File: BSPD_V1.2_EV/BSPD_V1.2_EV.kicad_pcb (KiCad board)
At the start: 2 copper layers, 82.1 x 92.5 mm, 64 parts, among them IC1 LM2901BIRTER, IC2 LM2901BIRTER, IC3 74AHC1G08, IC4 SN74HC32PWR, IC5 L7805ACD2T-TR, J1 776280-1, Q1 2N7002,215

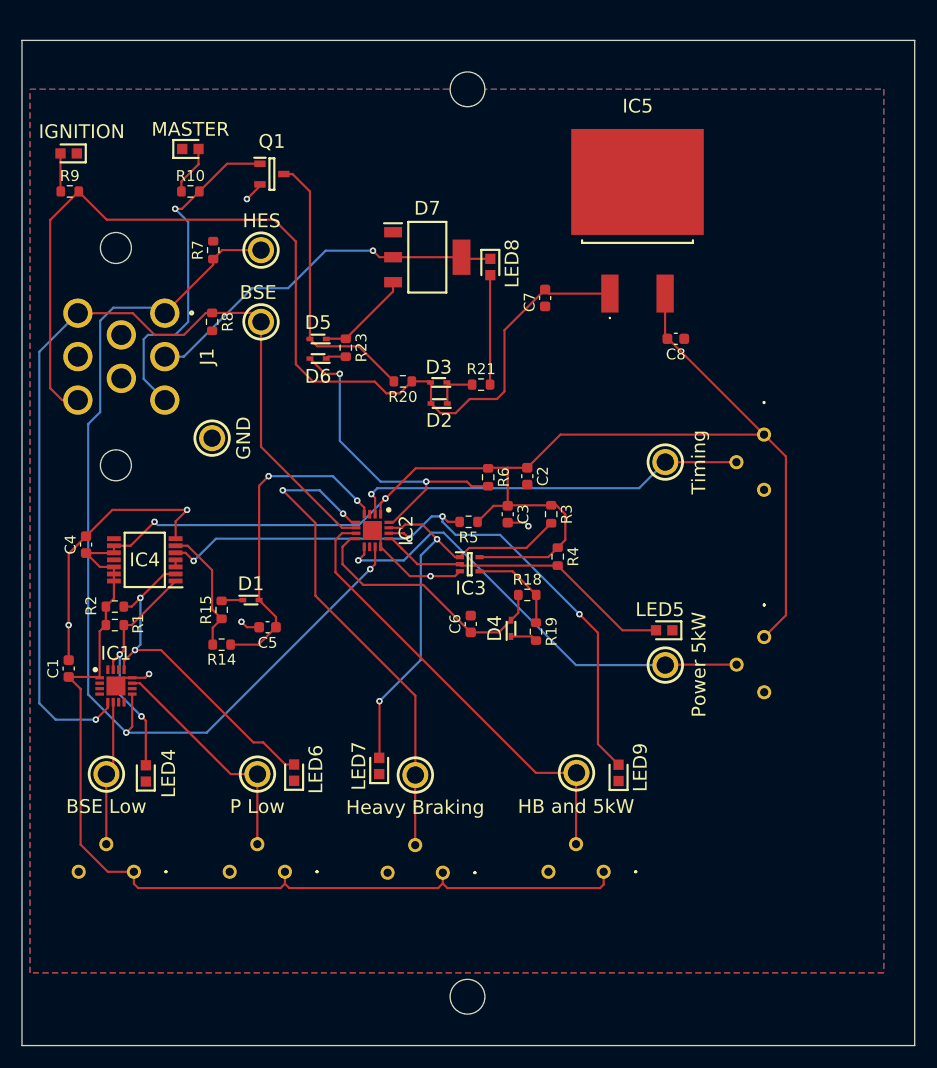
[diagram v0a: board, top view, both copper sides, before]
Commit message: BSPD, Shutdown/Charging Shutdown, & Voltage Indicator final changes
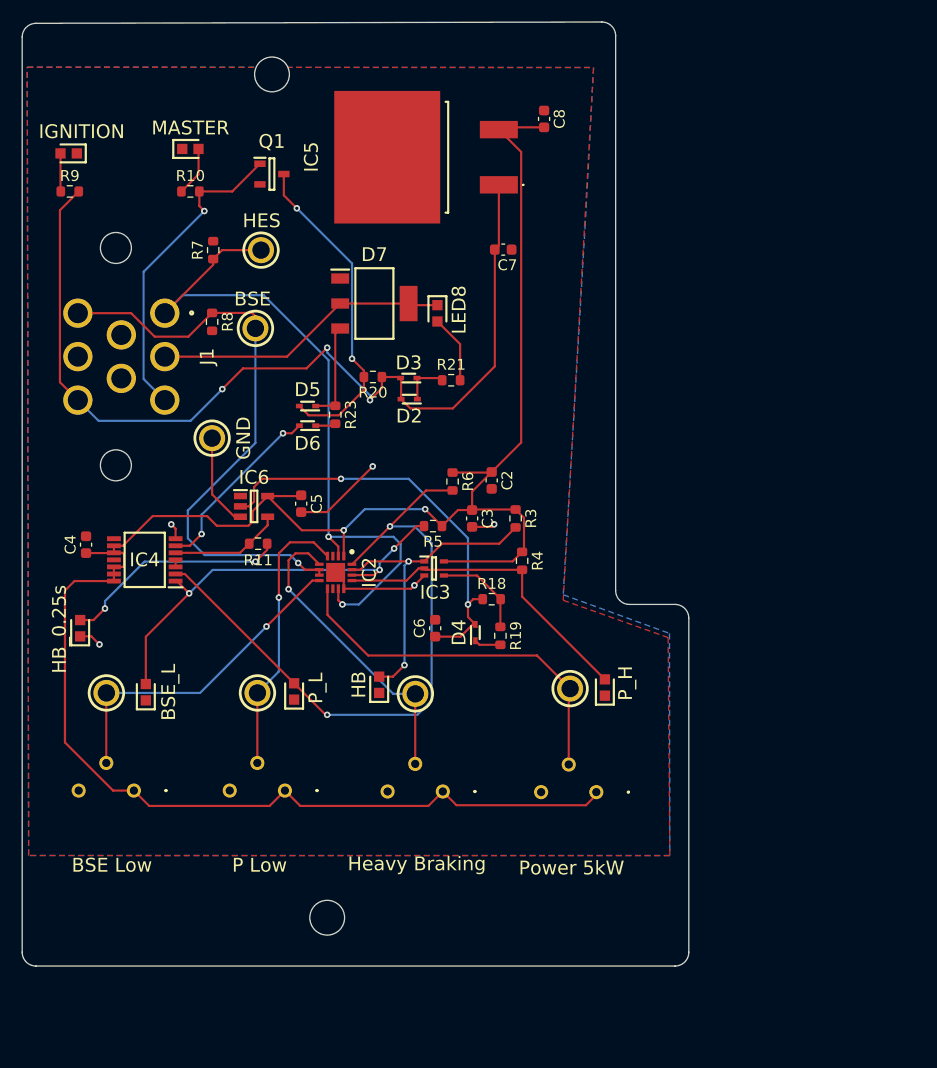
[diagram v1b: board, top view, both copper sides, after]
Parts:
- removed C1: 1uF, Capacitor_SMD:C_0603_1608Metric
- removed D1: BAT54XV2T1G, SDM_MiscFootprint:SODFL1608X70N
- removed IC1: LM2901BIRTER, SDM_MiscFootprint:QFN50P300X300X80-17N-D
- removed R1, R2: 220, Resistor_SMD:R_0603_1608Metric
- removed R14: 10k, Resistor_SMD:R_0603_1608Metric
- removed R15: 100, Resistor_SMD:R_0603_1608Metric
- removed RED_TP1, RED_TP2: 5005, SDM_MiscFootprint:5005
- removed the REF** at (102.7, 155.1)
- removed the REF** at (102.7, 71.6)
- removed VR1, VR2: 10k, SDM_MiscFootprint:3386P1103TLF
- added IC6: SN74LVC1G17DBVRG4, Misc:SOT95P280X145-5N, F.Cu at (83.1, 110.0)
- added R11: 220, Resistor_SMD:R_0603_1608Metric, F.Cu at (83.4, 113.4)
- added REF**: MountingHole_3.2mm_M3, MountingHole:MountingHole_3.2mm_M3, F.Cu at (84.7, 70.2)
- added REF**: MountingHole_3.2mm_M3, MountingHole:MountingHole_3.2mm_M3, F.Cu at (89.8, 147.8)
- C5: value 10uF -> 1uF
- R18: value 50k -> 25k
- moved HB_0.25s 51.3 mm to (67.1, 121.2)
- moved C8 23.6 mm to (109.7, 74.3), turned to -90 degrees
- moved VR3 21.0 mm to (114.6, 136.3), turned to 0 degrees
- moved IC5 20.5 mm to (98.7, 77.9), turned to 90 degrees
- moved C5 11.8 mm to (87.4, 109.7), turned to -90 degrees
- moved RED_TP3 9.02 mm to (112.1, 126.7), turned to 0 degrees
- moved P_H 7.58 mm to (115.3, 126.6), turned to 90 degrees
- moved BSE_L 7.47 mm to (73.1, 127.1)
- moved HB 7.47 mm to (94.6, 126.4)
- moved RED_TP5 7.47 mm to (83.4, 127.1)
- moved RED_TP6 7.47 mm to (69.5, 127.1)
- moved VR4 7.47 mm to (100.4, 136.2)
- moved VR5 7.47 mm to (85.9, 136.1)
- moved VR6 7.47 mm to (72.0, 136.1)
- moved P_L 7.47 mm to (86.7, 127.0)
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- renumbered LED4 to BSE_L, LED7 to HB, LED9 to HB_0.25s, LED5 to P_H, LED6 to P_L
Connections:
- C5 pad 1: /BL+PL+(HB*5kW)_FAULT -> +5V
- HB_0.25s pad 2: /HB*5kW_0.25s_FAULT -> Net-(LED9-A)
- IC2 pad 14: /HB*5kW_0.25s_FAULT -> /BSE_LOW_FAULT
- IC2 pad 16: /BSPD_LOGIC_SIGNAL -> /P_LOW_FAULT
- IC2 pad 2: /TIMING_REF -> /P_MAIN
- IC2 pad 4: /BL+PL+(HB*5kW)_FAULT -> /P_LOW_REF
- IC2 pad 7: /HB*5kW_REF -> /BSE
- IC2 pad 8: /HB*5kW_FAULT -> /BSE_LOW_REF
- IC4 pad 6: Net-(IC4-2Y) -> /BSPD_LOGIC_SIGNAL
- R5 pad 2: /HB*5kW_0.25s_FAULT -> /BSE_LOW_FAULT
- R6 pad 2: /BSPD_LOGIC_SIGNAL -> /P_LOW_FAULT
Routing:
- net /HB*5kW_0.25s_FAULT: track 62.4 -> 10.3 mm, vias 4 -> 0
- net /HB*5kW_REF: track 41.5 -> 0.00 mm
- net /TIMING_REF: track 36.8 -> 0.00 mm, vias 1 -> 0
- net /BSE: track 87.4 -> 55.2 mm
- net /BL+PL+(HB*5kW)_FAULT: track 30.3 -> 0.00 mm, vias 2 -> 0
- net +5V: track 216.8 -> 187.1 mm
- net /P_LOW_FAULT: track 32.2 -> 60.5 mm
- net /P_MAIN: track 92.7 -> 65.4 mm
- net Net-(LED9-A): track 0.00 -> 20.9 mm, vias 0 -> 2
- net /HEAVY_BRAKING_REF: track 45.7 -> 28.3 mm, vias 2 -> 1
- net /BSE_LOW_REF: track 13.3 -> 30.3 mm, vias 0 -> 1
- net /BSE_LOW_FAULT: track 22.1 -> 39.0 mm, vias 2 -> 3
- net /HB*5kW_FAULT: track 24.3 -> 39.0 mm, vias 0 -> 2
- net /BSPD_LOGIC_SIGNAL: track 30.3 -> 17.0 mm
- net GND: track 45.1 -> 32.4 mm, vias 7 -> 5
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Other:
- board size 82.1 x 92.5 mm -> 61.3 x 86.9 mm

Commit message: Fixed a net in BSPD and added isolated 5V line in voltage indicator
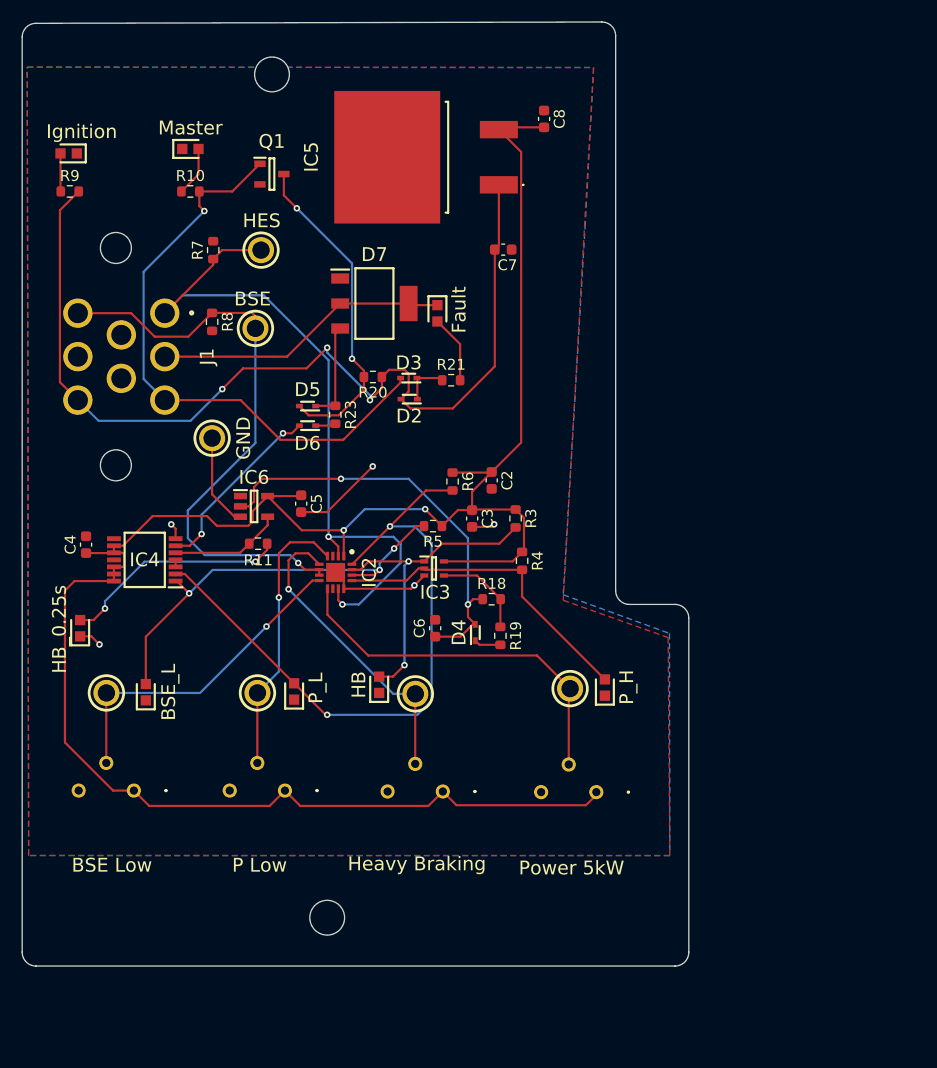
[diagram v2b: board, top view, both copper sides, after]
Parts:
- renumbered LED8 to Fault, IGNITION to Ignition, MASTER to Master
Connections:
- D3 pad 2: /12V IGNITION -> /12V MASTER
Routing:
- net /12V MASTER: track 29.1 -> 55.1 mm
- net /12V IGNITION: track 87.3 -> 89.1 mm
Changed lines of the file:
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@@
 			)
 		)
-		(property "Measure" "BSE"
-			(at 2.7 -1.966 0)
-			(unlocked yes)
-			(layer "F.SilkS")
-			(effects
-				(font
-					(size 1.27 1.27)
-					(thickness 0.254)
-				)
-				(justify left)
-			)
-		)
 		(property "Height" "5.59"
 			(at 0 0 90)
@@
 			)
 		)
+		(property "Measure" "BSE"
+			(at 2.7 -1.966 0)
+			(unlocked yes)
+			(layer "F.SilkS")
+			(effects
+				(font
+					(size 1.27 1.27)
+					(thickness 0.254)
+				)
+				(justify left)
+			)
+		)
 		(sheetname "/")
 		(sheetfile "BSPD_V1.2_EV.kicad_sch")
@@
 		(descr "WL-SMCW")
 		(tags "LED")
-		(property "Reference" "MASTER"
+		(property "Reference" "Master"
 			(at 0 -1.927 180)
 			(layer "F.SilkS")
@@
 		(descr "WL-SMCW")
 		(tags "LED")
-		(property "Reference" "LED8"
+		(property "Reference" "Fault"
 			(at -0.32 -2 90)
 			(layer "F.SilkS")
@@
 		(tags "LED")
 		(property "Reference" "P_H"
-			(at 0.4 1.9 90)
+			(at 0.027 2.007 90)
 			(layer "F.SilkS")
 			(effects
@@
 			(size 0.42 0.64)
 			(layers "F.Cu" "F.Mask" "F.Paste")
-			(net 5 "/12V IGNITION")
+			(net 32 "/12V MASTER")
 			(pinfunction "A")
 			(pintype "passive")
@@
 			)
 		)
-		(property "Measure" "GND"
-			(at 0 -2.9 90)
-			(layer "F.SilkS")
-			(effects
-				(font
-					(size 1.27 1.27)
-					(thickness 0.254)
-				)
-			)
-		)
 		(property "Height" "5.72"
 			(at 0 0 270)
@@
 			)
 		)
+		(property "Measure" "GND"
+			(at 0 -2.9 90)
+			(layer "F.SilkS")
+			(effects
+				(font
+					(size 1.27 1.27)
+					(thickness 0.254)
+				)
+			)
+		)
 		(sheetname "/")
 		(sheetfile "BSPD_V1.2_EV.kicad_sch")
@@
 		(descr "WL-SMCW")
 		(tags "LED")
-		(property "Reference" "IGNITION"
+		(property "Reference" "Ignition"
 			(at -1.2 2 0)
 			(layer "F.SilkS")
@@
 	)
 	(segment
-		(start 94.82 98.071)
-		(end 96.445 98.071)
+		(start 96.585 100.111)
+		(end 97.282 99.414)
 		(width 0.2)
 		(layer "F.Cu")
@@
 	)
 	(segment
-		(start 89.789 95.377)
-		(end 87.884 97.282)
+		(start 96.913 97.409)
+		(end 95.482 97.409)
 		(width 0.2)
 		(layer "F.Cu")
@@
 	)
 	(segment
-		(start 96.445 98.071)
-		(end 96.545 98.171)
+		(start 89.789 95.377)
+		(end 87.884 97.282)
 		(width 0.2)
 		(layer "F.Cu")
@@
 	)
 	(segment
-		(start 105.211 97.1)
-		(end 101.346 100.965)
+		(start 95.482 97.409)
+		(end 94.82 98.071)
 		(width 0.2)
 		(layer "F.Cu")
@@
 	)
 	(segment
-		(start 96.585 98.211)
-		(end 96.545 98.171)
+		(start 97.282 97.778)
+		(end 96.913 97.409)
+		(width 0.2)
+		(layer "F.Cu")
+		(net 5)
+	)
+	(segment
+		(start 105.211 97.1)
+		(end 101.346 100.965)
 		(width 0.2)
 		(layer "F.Cu")
@@
 	)
 	(segment
-		(start 96.585 100.111)
-		(end 96.585 98.211)
+		(start 65.19541 98.55)
+		(end 65.19541 82.72959)
 		(width 0.2)
 		(layer "F.Cu")
@@
 	)
 	(segment
-		(start 65.19541 98.55)
-		(end 65.19541 82.72959)
+		(start 97.282 99.414)
+		(end 97.282 97.778)
 		(width 0.2)
 		(layer "F.Cu")
@@
 	)
 	(segment
+		(start 96.445 98.071)
+		(end 96.545 98.171)
+		(width 0.2)
+		(layer "F.Cu")
+		(net 32)
+	)
+	(segment
+		(start 91.275 103.851)
+		(end 96.545 98.581)
+		(width 0.2)
+		(layer "F.Cu")
+		(net 32)
+	)
+	(segment
 		(start 78.025 81)
 		(end 78.025 82.343)
 		(width 0.2)
 		(layer "F.Cu")
+		(net 32)
+	)
+	(segment
+		(start 96.545 98.581)
+		(end 96.545 98.171)
+		(width 0.2)
+		(layer "F.Cu")
+		(net 32)
+	)
+	(segment
+		(start 96.585 98.211)
+		(end 96.545 98.171)
+		(width 0.2)
+		(layer "F.Cu")
+		(net 32)
+	)
+	(segment
+		(start 74.84541 100.2)
+		(end 81.825471 100.2)
+		(width 0.2)
+		(layer "F.Cu")
+		(net 32)
+	)
+	(segment
+		(start 85.476471 103.851)
+		(end 91.275 103.851)
+		(width 0.2)
+		(layer "F.Cu")
+		(net 32)
+	)
+	(segment
+		(start 81.825471 100.2)
+		(end 85.476471 103.851)
+		(width 0.2)
+		(layer "F.Cu")
